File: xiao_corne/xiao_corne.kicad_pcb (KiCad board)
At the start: 2 copper layers, 141 x 88.5 mm, 81 parts, among them J1 USB4110GFA, J6 Conn_01x04_Socket, SW1 SW_Push, SW11 SW_Push, SW12 SW_Push, SW13 SW_Push, SW14 SW_Push, SW15 SW_Push, SW2 SW_Push, SW21 SW_Push, SW22 SW_Push, SW23 SW_Push, SW24 SW_Push, SW25 SW_Push, SW3 SW_Push, SW31 SW_Push, SW32 SW_Push, SW33 SW_Push, SW34 SW_Push, SW35 SW_Push, SW4 SW_Push, SW41 SW_Push, SW5 SW_Push, SW6 SW_Push, U1 SN74AHCT125DR, U2 ESP32-S3-WROOM-1, U3 TPS61201DRCT, U4 BQ24232RGTR

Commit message: almost done routing left half!
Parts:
- C10, C11, C12, C13, C14, C15, C16, C3, C4, C7, C8, C9, D1, D16, D17, D18, D19, D2, D20, D21, D22, D23, D47, D48, D49, D50, D51, D52, D53, D54, D73, D74, D75, D76, D77, J1, L2, R1, R10, R2, R3, R4, R5, R6, R7, R8, R9, U1, U2, U3, U4: moved to B.Cu
- H1, H2, H3: footprint MountingHole:MountingHole_3.2mm_M3_ISO14580 -> MountingHole:MountingHole_2.2mm_M2_ISO14580_Pad_TopBottom
- moved D21 246.9 mm to (54.5, 76.7), turned to 180 degrees
- moved D50 238.7 mm to (54.5, 95.8), turned to 180 degrees
- moved D20 234.7 mm to (73.6, 76.7), turned to 180 degrees
- moved D74 234.5 mm to (54.5, 114.8), turned to 180 degrees
- moved D49 227.6 mm to (73.6, 95.8), turned to 180 degrees
- moved D73 224.8 mm to (73.6, 114.8), turned to 180 degrees
- moved R9 223.6 mm to (168.1, 73.6), turned to -90 degrees
- moved C15 222.7 mm to (159.1, 74.1), turned to 180 degrees
- moved R10 222.0 mm to (165.6, 70.1)
- moved D19 219.8 mm to (92.6, 72.0), turned to 180 degrees
- moved C14 219.0 mm to (168.1, 78.1), turned to -90 degrees
- moved U4 216.2 mm to (164.4, 74.5), turned to 180 degrees
- moved D48 213.6 mm to (92.6, 91.0), turned to 180 degrees
- moved D54 211.8 mm to (92.6, 110.1), turned to 180 degrees
- moved C16 210.4 mm to (161.1, 70.6), turned to 180 degrees
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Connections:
- net Net-(U2-GPIO19/U1RTS/ADC2_CH8/CLK_OUT2/USB_D-) renamed d-
- net Net-(U2-GPIO20/U1CTS/ADC2_CH9/CLK_OUT1/USB_D+) renamed d+
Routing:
- net +4.4V L: track 0.00 -> 494.8 mm
- net Net-(D74-DOUT): track 0.00 -> 147.4 mm
- net KS_L7: track 0.00 -> 141.6 mm, vias 0 -> 2
- net KS_L3: track 0.00 -> 141.4 mm, vias 0 -> 2
- net KS_L11: track 0.00 -> 129.4 mm, vias 0 -> 2
- net KS_L2: track 0.00 -> 127.2 mm, vias 0 -> 2
- net KS_L4: track 0.00 -> 119.2 mm, vias 0 -> 2
- net KS_L12: track 0.00 -> 113.4 mm, vias 0 -> 2
- net KS_L19: track 0.00 -> 102.2 mm, vias 0 -> 2
- net KS_L5: track 0.00 -> 101.8 mm, vias 0 -> 2
- net KS_L13: track 0.00 -> 89.9 mm, vias 0 -> 2
- net KS_L6: track 0.00 -> 88.2 mm, vias 0 -> 2
- net KS_L8: track 0.00 -> 77.5 mm, vias 0 -> 2
- net KS_L14: track 0.00 -> 72.1 mm, vias 0 -> 2
- net KS_L16: track 0.00 -> 64.9 mm, vias 0 -> 2
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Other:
- outline, holes or cut-outs redrawn

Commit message: ready for review
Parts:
- removed the G*** at (254.9, 204.8)
- removed the G*** at (287.6, 204.4)
- added G***: LOGO, LOGO, F.Cu at (170.8, 99.4)
- moved C3 35.7 mm to (156.7, 96.9), turned to 0 degrees
- moved C4 35.6 mm to (158.0, 111.0), turned to 0 degrees
- moved C7 35.6 mm to (158.0, 114.0)
- moved R7 35.5 mm to (156.7, 93.9), turned to 0 degrees
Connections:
- U2 pad 1: GND -> GND L
- U2 pad 39: BAT/2 MON L -> unconnected-(U2-GPIO1/TOUCH1/ADC1_CH0-Pad39)
- U2 pad 40: GND -> GND L
- U2 pad 41: GND -> GND L
- U3 pad 11: unconnected-(U3-EP-Pad11) -> (no net)
- U4 pad 4: GND -> GND L
- U4 pad V: (no net) -> GND L
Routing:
- net +3.3V L: track 3.40 -> 325.4 mm, vias 0 -> 14
- net GND L: track 0.00 -> 264.1 mm, vias 0 -> 16
- net Net-(D50-DOUT): track 0.00 -> 126.5 mm
- net Net-(D21-DOUT): track 0.00 -> 122.9 mm
- net (no net): track 58.0 -> 0.00 mm
- net LED_5v L: track 0.00 -> 46.1 mm, vias 0 -> 2
- net BAT/2 MON L: track 7.27 -> 52.5 mm, vias 0 -> 2
- net pgood L: track 1.20 -> 46.1 mm, vias 0 -> 4
- net Net-(U2-EN): track 0.00 -> 27.8 mm, vias 0 -> 2
- net VUSB L: track 25.1 -> 46.4 mm
- net +4.4V L: track 494.8 -> 513.8 mm, vias 0 -> 2
- net KS_L10: track 32.2 -> 34.2 mm
- net KS_L15: track 64.9 -> 65.6 mm
- net VBAT L: track 22.3 -> 23.0 mm
- added copper zone on F.Cu, net +3.3V L
- added copper zone on B.Cu, net GND L
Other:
- outline, holes or cut-outs redrawn

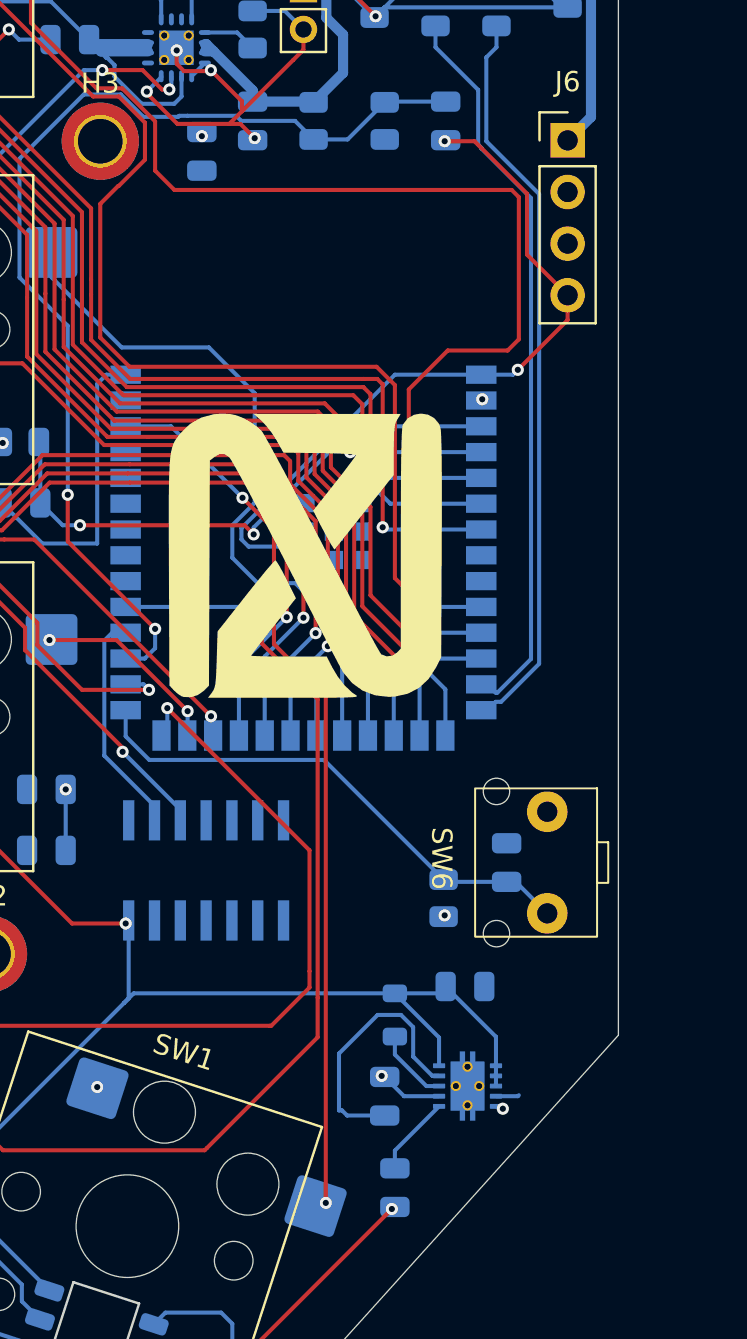
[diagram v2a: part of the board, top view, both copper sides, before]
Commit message: changed 3.3v regulator to step down from step up converter
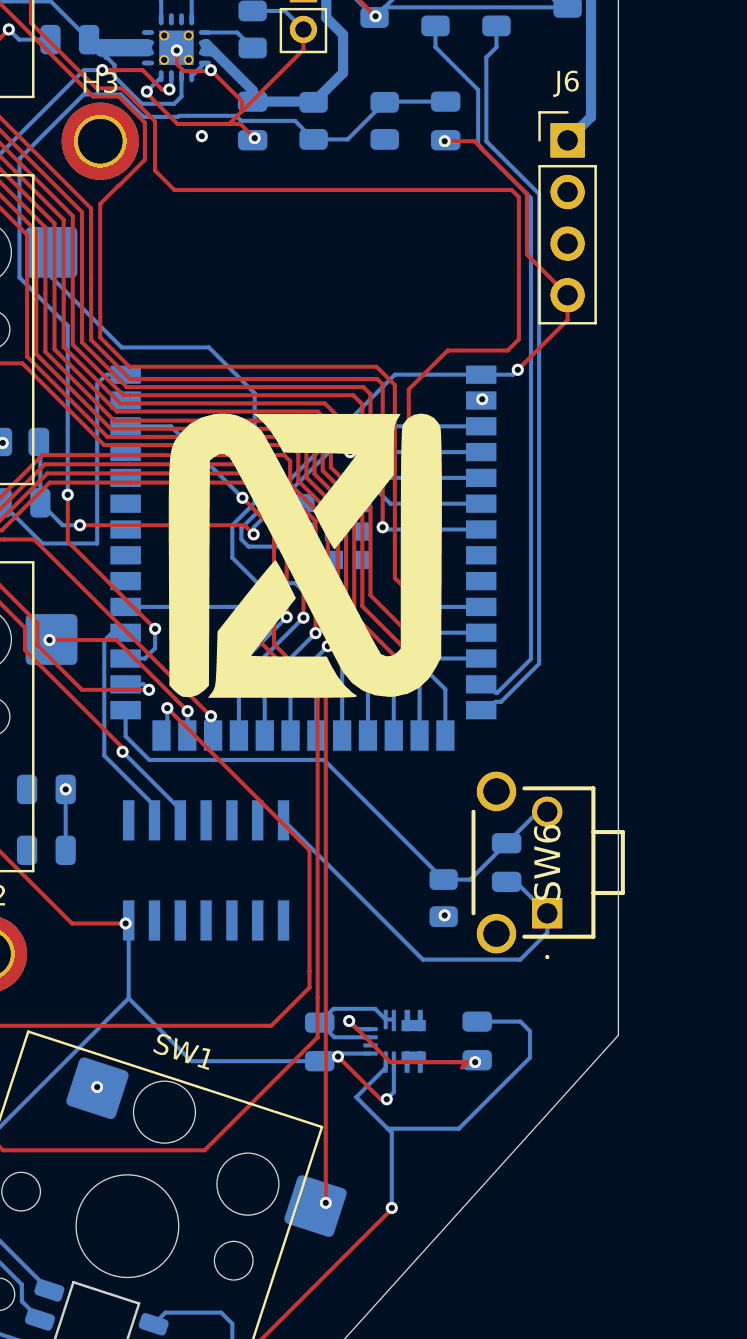
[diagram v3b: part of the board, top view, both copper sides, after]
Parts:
- removed C10, C12, C13: 10uF, Capacitor_SMD:C_0805_2012Metric
- removed C11: 0.1uF, Capacitor_SMD:C_0805_2012Metric
- removed L2: 2.2uH, Inductor_SMD:L_0805_2012Metric
- removed U3: TPS61201DRCT, TPS61201DRCT:VREG_V62_16624-01YE
- added C1: 10uF, Capacitor_SMD:C_0805_2012Metric, B.Cu at (171.4, 123.5)
- added C2: 10uF, Capacitor_SMD:C_0805_2012Metric, B.Cu at (179.2, 123.4)
- added U5: MPM3810GQB-33-Z, footprints_mpm:QFN-12_MPM3810_MNP, B.Cu at (175.4, 123.4)
- SW6: footprint footprints:MJTP1117 -> MJTP1117:MJTP1117
- moved SW6 2.50 mm to (182.6, 117.1), turned to 90 degrees
- turned C8 to -90 degrees
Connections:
- U4 pad V: GND L -> (no net)
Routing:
- net GND L: track 264.1 -> 298.0 mm
- net +3.3V L: track 325.4 -> 333.8 mm
- net +4.4V L: track 513.8 -> 506.8 mm, vias 2 -> 4
- net Net-(U3-VAUX): track 3.95 -> 0.00 mm
- net Net-(U3-L): track 3.70 -> 0.00 mm
- net Net-(U2-GPIO0/BOOT): track 25.7 -> 26.6 mm

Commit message: ordered!
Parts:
- moved H3 3.06 mm to (163.4, 80.5)
- moved S1 2.40 mm to (165.7, 63.2)
- moved J1 1.60 mm to (177.6, 65.0)
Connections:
- U5 pad 8: GND L -> unconnected-(U5-PG-Pad8)
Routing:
- net GND L: track 298.0 -> 293.4 mm
- net Net-(J1-DP1): track 7.50 -> 10.4 mm
- net VUSB L: track 46.4 -> 49.3 mm
- net KS_L14: track 72.0 -> 69.4 mm
- net Net-(BT1-+): track 9.39 -> 11.8 mm
- net VBAT L: track 23.0 -> 25.4 mm
- net KS_L15: track 65.6 -> 63.6 mm
- net Net-(J1-CC2): track 5.22 -> 6.80 mm
- net Net-(J1-DN1): track 7.48 -> 8.80 mm
- net Net-(J1-CC1): track 5.40 -> 6.07 mm
- net +3.3V L: track 333.8 -> 333.6 mm, vias 14 -> 13
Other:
- board size 141 x 88.5 mm -> 141 x 88.1 mm

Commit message: Fixed issue with battery monitor
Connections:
- U2 pad 29: BAT/2 MON L -> unconnected-(U2-SPIIO7/GPIO36/FSPICLK/SUBSPICLK-Pad29)
- U2 pad 39: unconnected-(U2-GPIO1/TOUCH1/ADC1_CH0-Pad39) -> BAT/2 MON L
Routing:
- net BAT/2 MON L: track 52.5 -> 40.6 mm, vias 2 -> 0

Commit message: got right side components flipped and generally correct
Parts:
- moved D21 291.0 mm to (345.5, 76.7)
- moved D50 291.0 mm to (345.5, 95.8)
- moved D74 291.0 mm to (345.5, 114.8)
- moved SW12 291.0 mm to (345.5, 90.8)
- moved SW21 291.0 mm to (345.5, 109.8)
- moved SW3 291.0 mm to (345.5, 71.7)
- moved H1 271.8 mm to (335.9, 81.2)
- moved D20 252.9 mm to (326.4, 76.7)
- moved D49 252.9 mm to (326.4, 95.8)
- moved D73 252.9 mm to (326.4, 114.8)
- moved SW2 252.9 mm to (326.4, 90.8)
- moved SW22 252.9 mm to (326.4, 109.8)
- moved SW4 252.9 mm to (326.4, 71.7)
- moved D19 214.9 mm to (307.4, 72.0)
- moved D48 214.9 mm to (307.4, 91.0)
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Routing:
- net +4.4V L: track 506.8 -> 0.00 mm, vias 4 -> 0
- net +3.3V L: track 333.6 -> 0.00 mm, vias 13 -> 0
- net Net-(D74-DOUT): track 147.1 -> 0.00 mm
- net Net-(D50-DOUT): track 126.5 -> 0.00 mm
- net Net-(D21-DOUT): track 122.9 -> 0.00 mm
- net KS_L4: track 119.2 -> 0.00 mm, vias 2 -> 0
- net KS_L5: track 101.8 -> 0.00 mm, vias 2 -> 0
- net KS_L6: track 88.2 -> 0.00 mm, vias 2 -> 0
- net KS_L14: track 69.4 -> 0.00 mm, vias 2 -> 0
- net KS_L15: track 63.6 -> 0.00 mm, vias 2 -> 0
- net KS_L18: track 60.4 -> 0.00 mm, vias 2 -> 0
- net GND L: track 293.4 -> 234.1 mm, vias 16 -> 0
- net KS_L17: track 52.8 -> 0.00 mm, vias 2 -> 0
- net VUSB L: track 49.3 -> 0.00 mm
- net LED_5v L: track 46.1 -> 0.00 mm, vias 2 -> 0
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- removed copper zone on F.Cu, net +3.3V L
- removed copper zone on B.Cu, net GND L
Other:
- outline, holes or cut-outs redrawn

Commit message: right PCB ready for final review!
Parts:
- moved R6 9.78 mm to (216.1, 72.6), turned to -90 degrees
- moved R5 9.29 mm to (225.6, 72.6), turned to -90 degrees
- moved R9 8.74 mm to (240.6, 73.6)
- moved C2 5.67 mm to (224.6, 127.6), turned to 0 degrees
- moved C8 4.97 mm to (224.1, 116.1)
- moved R8 4.64 mm to (227.1, 116.1)
- moved R7 3.89 mm to (242.1, 97.6), turned to 180 degrees
- moved C15 3.51 mm to (240.6, 77.6), turned to 90 degrees
- moved C3 2.56 mm to (242.2, 94.6), turned to 180 degrees
- moved C4 1.65 mm to (241.6, 112.6)
- moved C7 1.65 mm to (241.6, 115.6)
- moved R10 0.50 mm to (234.4, 69.6), turned to 180 degrees
- turned C16 to 0 degrees
- turned D1 to 0 degrees
- turned D16 to 0 degrees
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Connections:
- U4 pad V: (no net) -> GND L
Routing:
- net +4.4V L: track 0.00 -> 499.0 mm, vias 0 -> 5
- net +3.3V L: track 0.00 -> 202.8 mm, vias 0 -> 24
- net Net-(D74-DOUT): track 0.00 -> 133.9 mm
- net Net-(D50-DOUT): track 0.00 -> 125.9 mm
- net Net-(D21-DOUT): track 0.00 -> 123.7 mm
- net KS_L4: track 0.00 -> 117.8 mm, vias 0 -> 2
- net GND L: track 234.1 -> 128.2 mm, vias 0 -> 16
- net KS_L5: track 0.00 -> 100.7 mm, vias 0 -> 2
- net KS_L6: track 0.00 -> 85.5 mm, vias 0 -> 2
- net KS_L18: track 0.00 -> 75.8 mm, vias 0 -> 2
- net KS_L14: track 0.00 -> 72.6 mm, vias 0 -> 2
- net KS_L17: track 0.00 -> 60.9 mm, vias 0 -> 2
- net KS_L15: track 0.00 -> 55.4 mm, vias 0 -> 2
- net KS_L20: track 15.9 -> 67.5 mm, vias 0 -> 2
- net LED_5v L: track 0.00 -> 48.3 mm, vias 0 -> 2
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- added copper zone on F.Cu, net +3.3V L
- added copper zone on B.Cu, net GND L

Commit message: Right side ordered!
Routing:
- net Net-(D20-DOUT): track 14.5 -> 15.2 mm
